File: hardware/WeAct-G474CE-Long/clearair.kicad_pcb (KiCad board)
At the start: 2 copper layers, 116.8 x 58.4 mm, 35 parts, among them J3 SPS30, J4 BME680, J5 MQ131, J6 MiCS-4514, J7 RTC PCF8563, M2 80mm fan front, M3 80mm fan rear, Q1 2N7000, Q2 2N7000, Q3 2N2222A, SW1 RESET red, SW2 COLD_BOOT white, U5 RobotDyn AC dimmer

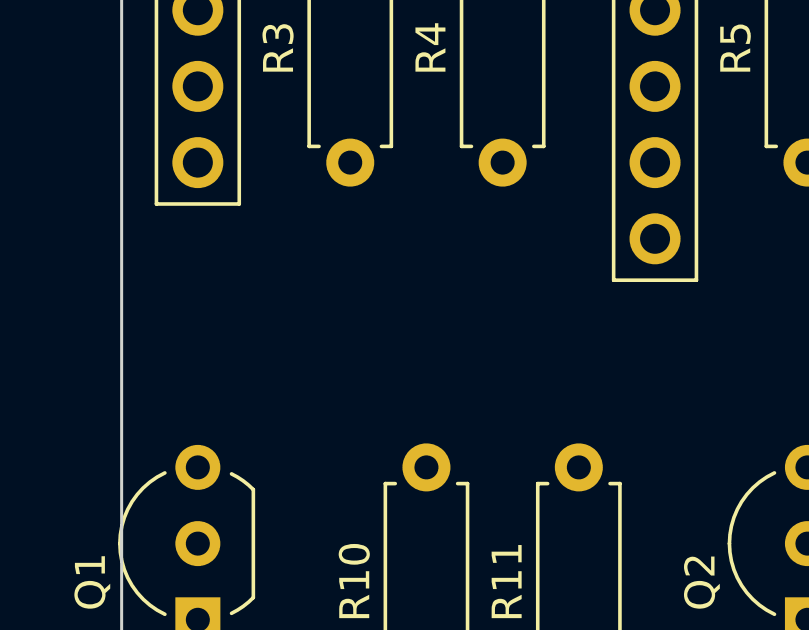
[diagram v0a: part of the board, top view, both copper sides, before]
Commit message: add missing J8
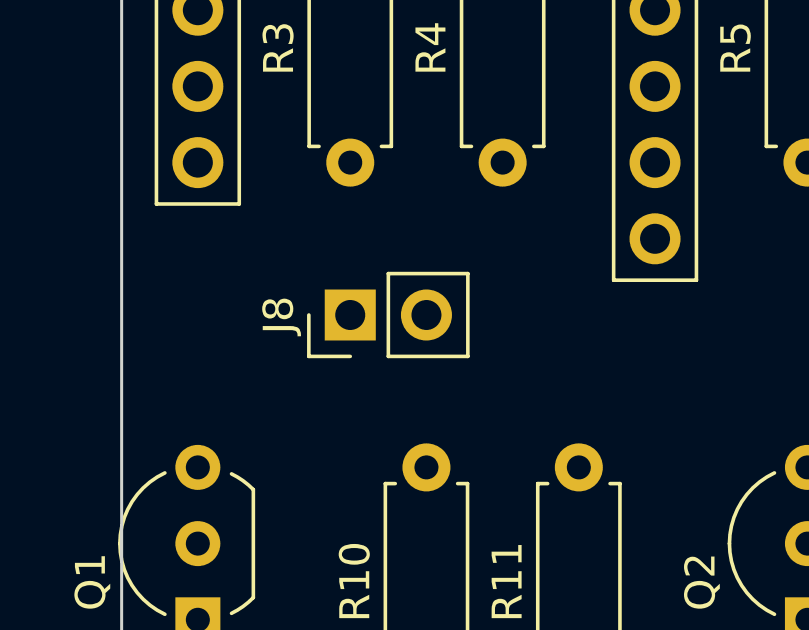
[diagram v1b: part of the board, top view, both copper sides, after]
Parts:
- added J8: Arduino, Connector_PinHeader_2.54mm:PinHeader_1x02_P2.54mm_Vertical, F.Cu at (111.8, 88.9)
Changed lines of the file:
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@@
+		)
+	)
+	(footprint "Connector_PinHeader_2.54mm:PinHeader_1x02_P2.54mm_Vertical"
+		(layer "F.Cu")
+		(at 111.76 88.9 90)
+		(descr "Through hole straight pin header, 1x02, 2.54mm pitch, single row")
+		(tags "Through hole pin header THT 1x02 2.54mm single row")
+		(property "Reference" "J8"
+			(at 0 -2.38 90)
+			(layer "F.SilkS")
+			(effects
+				(font
+					(size 1 1)
+					(thickness 0.15)
+				)
+			)
+		)
+		(property "Value" "Arduino"
+			(at 0 4.92 90)
+			(layer "F.Fab")
+			(effects
+				(font
+					(size 1 1)
+					(thickness 0.15)
+				)
+			)
+		)
+		(property "Datasheet" ""
+			(at 0 0 90)
+			(layer "F.Fab")
+			(hide yes)
+			(effects
+				(font
+					(size 1.27 1.27)
+				)
+			)
+		)
+		(property "Description" "Header to the future Arduino display (Nano A2): 1 Display TX (to Arduino RX), 2 Display RX (from Arduino TX). 5V and GND go straight from the power supply."
+			(at 0 0 90)
+			(layer "F.Fab")
+			(hide yes)
+			(effects
+				(font
+					(size 1.27 1.27)
+				)
+			)
+		)
+		(property "KiLib_Generator" "connector/pin_header_socket"
+			(at 0 0 90)
+			(layer "F.SilkS")
+			(hide yes)
+			(effects
+				(font
+					(size 1 1)
+					(thickness 0.15)
+				)
+			)
+		)
+		(property "ki_keywords" "quartz resonator ceramic"
+			(at 0 0 90)
+			(unlocked yes)
+			(layer "F.Fab")
+			(hide yes)
+			(effects
+				(font
+					(size 1 1)
+					(thickness 0.15)
+				)
+			)
+		)
+		(property ki_fp_filters "*Buzzer*")
+		(sheetname "/")
+		(sheetfile "clearair.kicad_sch")
+		(units
+			(unit
+				(name "A")
+				(pins "1" "2")
+			)
+		)
+		(attr through_hole)
+		(duplicate_pad_numbers_are_jumpers no)
+		(fp_line
+			(start -1.38 -1.38)
+			(end 0 -1.38)
+			(stroke
+				(width 0.12)
+				(type solid)
+			)
+			(layer "F.SilkS")
+		)
+		(fp_line
+			(start -1.38 0)
+			(end -1.38 -1.38)
+			(stroke
+				(width 0.12)
+				(type solid)
+			)
+			(layer "F.SilkS")
+		)
+		(fp_line
+			(start 1.38 1.27)
+			(end 1.38 3.92)
+			(stroke
+				(width 0.12)
+				(type solid)
+			)
+			(layer "F.SilkS")
+		)
+		(fp_line
+			(start -1.38 1.27)
+			(end 1.38 1.27)
+			(stroke
+				(width 0.12)
+				(type solid)
+			)
+			(layer "F.SilkS")
+		)
+		(fp_line
+			(start -1.38 1.27)
+			(end -1.38 3.92)
+			(stroke
+				(width 0.12)
+				(type solid)
+			)
+			(layer "F.SilkS")
+		)
+		(fp_line
+			(start -1.38 3.92)
+			(end 1.38 3.92)
+			(stroke
+				(width 0.12)
+				(type solid)
+			)
+			(layer "F.SilkS")
+		)
+		(fp_rect
+			(start -1.77 -1.77)
+			(end 1.77 4.32)
+			(stroke
+				(width 0.05)
+				(type solid)
+			)
+			(fill no)
+			(layer "F.CrtYd")
+		)
+		(fp_line
+			(start 1.27 -1.27)
+			(end 1.27 3.81)
+			(stroke
+				(width 0.1)
+				(type solid)
+			)
+			(layer "F.Fab")
+		)
+		(fp_line
+			(start -0.635 -1.27)
+			(end 1.27 -1.27)
+			(stroke
+				(width 0.1)
+				(type solid)
+			)
+			(layer "F.Fab")
+		)
+		(fp_line
+			(start -1.27 -0.635)
+			(end -0.635 -1.27)
+			(stroke
+				(width 0.1)
+				(type solid)
+			)
+			(layer "F.Fab")
+		)
+		(fp_line
+			(start 1.27 3.81)
+			(end -1.27 3.81)
+			(stroke
+				(width 0.1)
+				(type solid)
+			)
+			(layer "F.Fab")
+		)
+		(fp_line
+			(start -1.27 3.81)
+			(end -1.27 -0.635)
+			(stroke
+				(width 0.1)
+				(type solid)
+			)
+			(layer "F.Fab")
+		)
+		(fp_text user "${REFERENCE}"
+			(at 0 1.27 0)
+			(layer "F.Fab")
+			(effects
+				(font
+					(size 1 1)
+					(thickness 0.15)
+				)
+			)
+		)
+		(pad "1" thru_hole rect
+			(at 0 0 90)
+			(size 1.7 1.7)
+			(drill 1)
+			(layers "*.Cu" "*.Mask")
+			(remove_unused_layers no)
+			(net "Net-(Q1-D)")
+			(pinfunction "Pin_1")
+			(pintype "passive")
+		)
+		(pad "2" thru_hole circle
+			(at 0 2.54 90)
+			(size 1.7 1.7)
+			(drill 1)
+			(layers "*.Cu" "*.Mask")
+			(remove_unused_layers no)
+			(net "Net-(Q2-D)")
+			(pinfunction "Pin_2")
+			(pintype "passive")
+		)
+		(embedded_fonts no)
+		(model "${KICAD10_3DMODEL_DIR}/Connector_PinHeader_2.54mm.3dshapes/PinHeader_1x02_P2.54mm_Vertical.step"
+			(offset
+				(xyz 0 0 0)
+			)
+			(scale
+				(xyz 1 1 1)
+			)
+			(rotate
+				(xyz 0 0 0)
+			)
 		)
 	)

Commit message: make kicad standard, make wire_list.py a generic script
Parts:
- added BUS1: +12V bus, clearair:Bus_Strip, F.Cu at (190.5, 99.1)
- added BUS2: +5V bus, clearair:Bus_Strip, F.Cu at (121.9, 66.0)
- added BUS3: +5V bus, clearair:Bus_Strip, F.Cu at (190.5, 73.7)
- added BUS4: +3V3 bus, clearair:Bus_Strip, F.Cu at (121.9, 71.1)
- added BUS5: +3V3 bus, clearair:Bus_Strip, F.Cu at (190.5, 114.3)
- added BUS6: GND bus, clearair:Bus_Strip, F.Cu at (121.9, 61.0)
- added BUS7: GND bus, clearair:Bus_Strip, F.Cu at (185.4, 94.0)

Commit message: finalize kicad standards
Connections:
- net Net-(A1-NRST) renamed /NRST
- net Net-(A1-PA0) renamed /MQ131_ADC
- net Net-(A1-PA1) renamed /MICS_CO1
- net Net-(A1-PA15) renamed /I2C_SCL
- net Net-(A1-PA5) renamed /FAN_FRONT_TACH
- net Net-(A1-PA7) renamed /MICS_NO2
- net Net-(A1-PA8) renamed /FAN_FRONT_PWM
- net Net-(A1-PA9) renamed /FAN_REAR_PWM
- net Net-(A1-PB0) renamed /ZC_INPUT
- net Net-(A1-PB1) renamed /TRIAC_DIMMER
- net Net-(A1-PB10) renamed /DISPLAY_TX
- net Net-(A1-PB11) renamed /DISPLAY_RX
- net Net-(A1-PB14) renamed /BOOT_MODE
- net Net-(A1-PB15) renamed /BUZZER_IN
- net Net-(A1-PB3) renamed /FAN_REAR_TACH
- net Net-(A1-PB7) renamed /I2C_SDA
- net Net-(BZ1--) renamed /BUZZER_NEG
- net Net-(J5-Pin_4) renamed /MQ131_OUT
- net Net-(J6-Pin_3) renamed /MICS_CO_OUT
- net Net-(J6-Pin_4) renamed /MICS_NO2_OUT
- net Net-(M2-Pin_4) renamed /FAN_FRONT_PWM_IN
- net Net-(M3-Pin_4) renamed /FAN_REAR_PWM_IN
- net Net-(Q1-D) renamed /DISPLAY_TX_5V
- net Net-(Q2-D) renamed /DISPLAY_RX_5V
- net Net-(Q3-B) renamed /BUZZER_BASE
- net Net-(U5-Z-C) renamed /ZC_OUT
